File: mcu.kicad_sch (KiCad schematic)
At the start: 26 parts, among them J1 Debugger, J5 UART, J7 GPIO, SW1 BOOT, U1 STM32F103C8Tx, U2 SN65HVD230, Y1 8 Mhz 5032

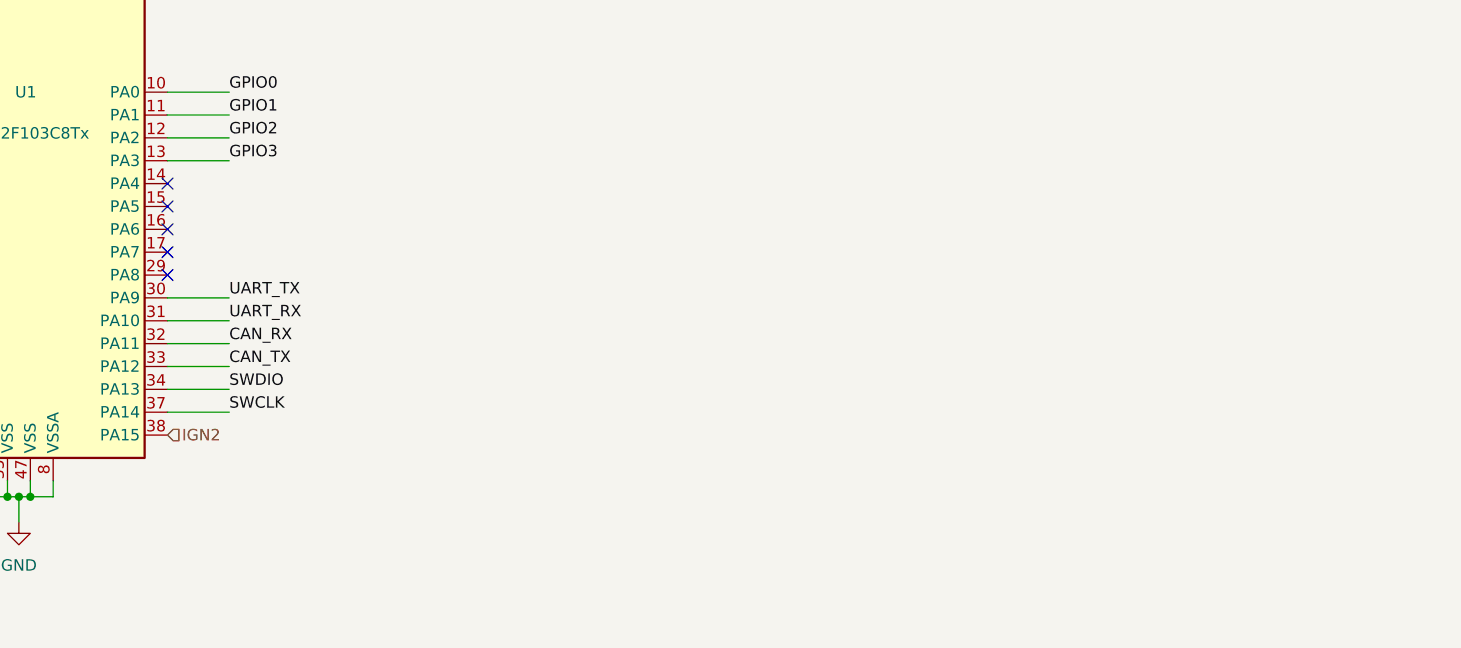
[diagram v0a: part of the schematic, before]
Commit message: Add pressure sensor schema and pcb layout for pyro and reverse polarity
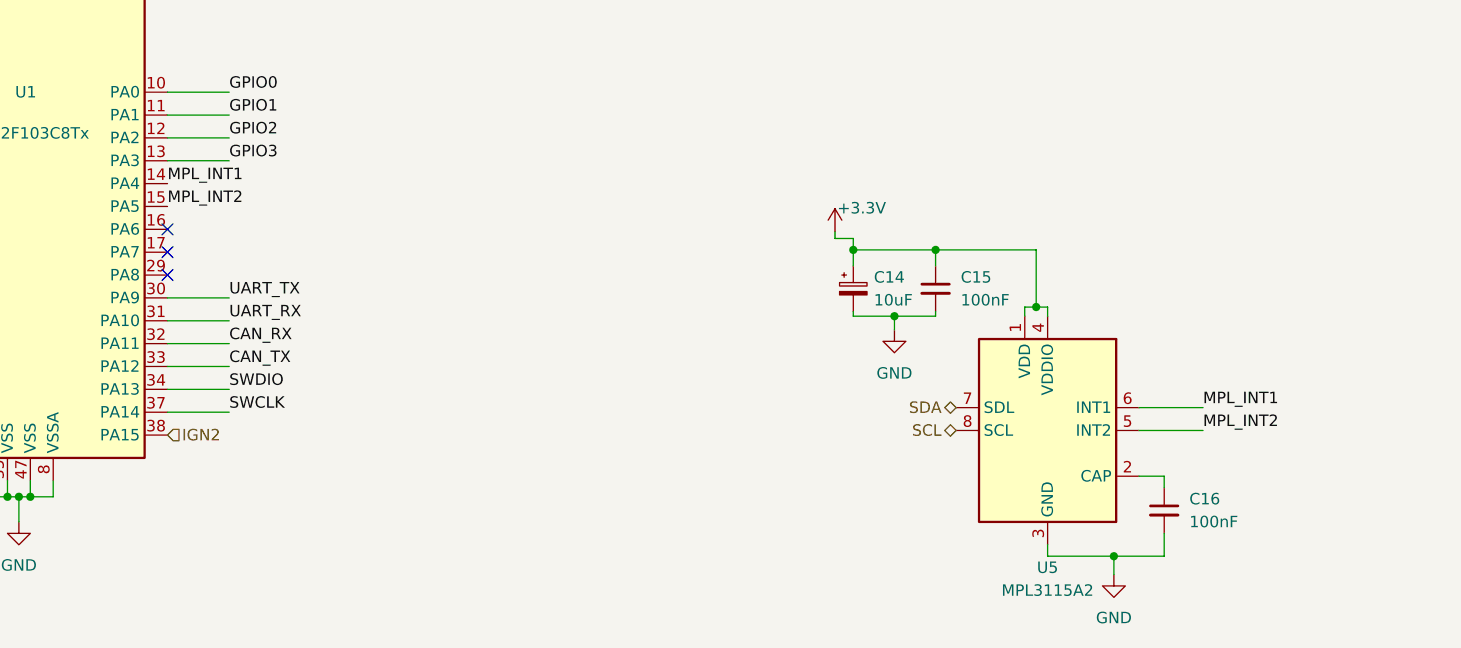
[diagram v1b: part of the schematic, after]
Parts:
- added C14: 10uF, Capacitor_Tantalum_SMD:CP_EIA-3216-18_Kemet-A, symbol Device:C_Polarized_Small
- added C15, C16: 100nF, Capacitor_SMD:C_0402_1005Metric, symbol Device:C_Small
- added U5: MPL3115A2, Package_LGA:NXP_LGA-8_3x5mm_P1.25mm_H1.1mm, symbol Sensor_Pressure:MPL3115A2
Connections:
- net +3V3: now also C14.1, C15.1, U5.1 (VDD), U5.4 (VDDIO)
- net GND: now also C14.2, C15.2, C16.2, U5.3 (GND)
- net SCL: now also U5.8 (SCL)
- net SDA: now also U5.7 (SDL)
- net MPL_INT1: now reaches U1.14 (PA4)
- net MPL_INT1: now also U5.6 (INT1)
- net MPL_INT2: now reaches U1.15 (PA5)
- net MPL_INT2: now also U5.5 (INT2)
- new net: C16.1, U5.2 (CAP)
- no-connect marks 14 -> 12

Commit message: Finish pcb layout for rev4
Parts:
- added R? (x2): 10k, Resistor_SMD:R_0402_1005Metric, symbol Device:R_Small
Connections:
- net +3V3: now also R?.1, R?.1
- net SCL: now also R?.2
- net SDA: now also R?.2
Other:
- moved on the sheet: C14, C15, C16, U5

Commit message: Generate gerber file
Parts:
- gave numbers to parts that had none: 2
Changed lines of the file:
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@@
   (symbol (lib_id "Device:R_Small") (at 207.518 135.382 0) (unit 1)
     (in_bom yes) (on_board yes) (fields_autoplaced)
-    (property "Reference" "R?" (id 0) (at 209.042 134.1119 0)
+    (property "Reference" "R17" (id 0) (at 209.042 134.1119 0)
       (effects (font (size 1.27 1.27)) (justify left))
     )
@@
   (symbol (lib_id "Device:R_Small") (at 215.392 135.382 0) (unit 1)
     (in_bom yes) (on_board yes) (fields_autoplaced)
-    (property "Reference" "R?" (id 0) (at 216.916 134.1119 0)
+    (property "Reference" "R18" (id 0) (at 216.916 134.1119 0)
       (effects (font (size 1.27 1.27)) (justify left))
     )
